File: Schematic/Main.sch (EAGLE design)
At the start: 48 parts, among them IC1 PIC18F4550_40, IC2 7805, IC4 AD7734, IC5 AD780, K1 SRD-24VDC-SL-C, K2 SRD-24VDC-SL-C, Q1 20MHz, Q2 6.144MHz, T1 2N2222, U1 LM317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

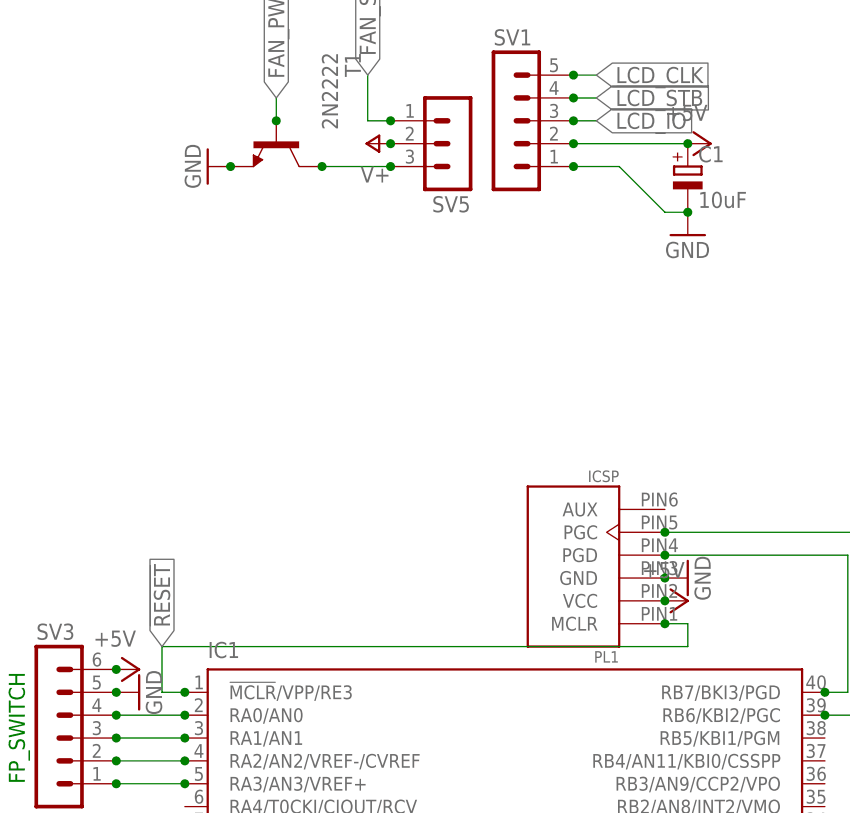
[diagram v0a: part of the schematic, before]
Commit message: Made some changes to capacitor values and such.g
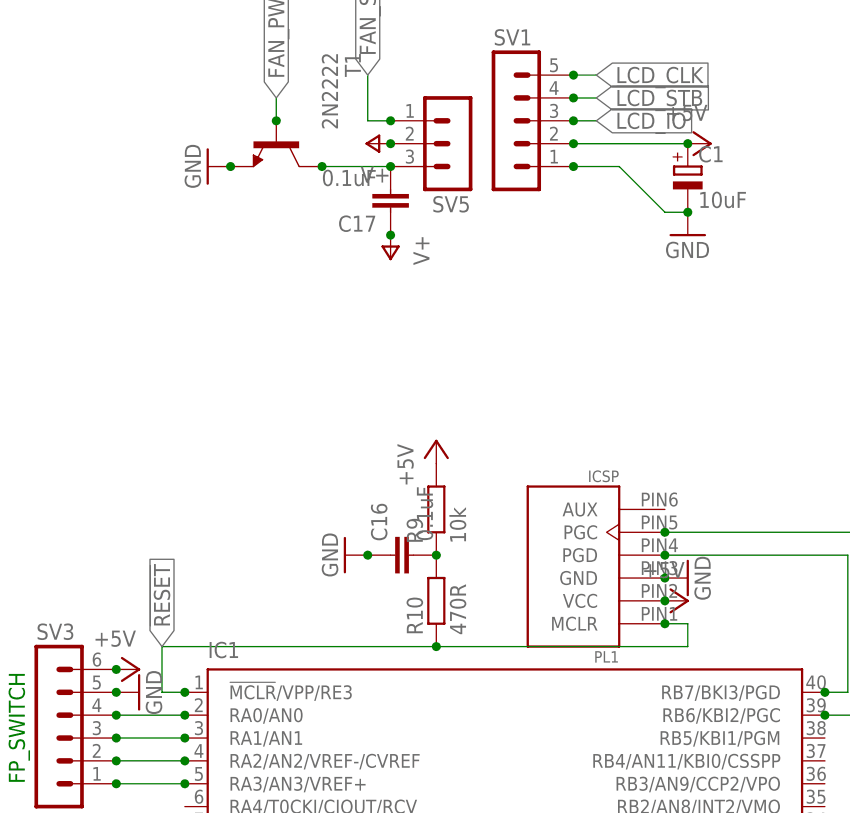
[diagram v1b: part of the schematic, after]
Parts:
- added C16, C17: 0.1uF, rcl:C-EU025-030X050
- added R10: 470R, rcl:R-EU_0204/7
- added R9: 10k, rcl:R-EU_0204/7
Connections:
- new net N$2: C16.2, R10.2, R9.1
- net !RESET!: now also R10.1
- net +5V: now also R9.2
- net GND: now also C16.1
- net N$27: now also C17.2
- net V+: now also C17.1
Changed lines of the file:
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@@
 <part name="AGND7" library="supply1" deviceset="AGND" device=""/>
 <part name="P+18" library="supply1" deviceset="+5V" device=""/>
+<part name="R9" library="rcl" deviceset="R-EU_" device="0204/7" value="10k"/>
+<part name="P+19" library="supply1" deviceset="+5V" device=""/>
+<part name="C17" library="rcl" deviceset="C-EU" device="025-030X050" value="0.1uF"/>
+<part name="P+20" library="supply1" deviceset="V+" device=""/>
+<part name="R10" library="rcl" deviceset="R-EU_" device="0204/7" value="470R"/>
+<part name="C16" library="rcl" deviceset="C-EU" device="025-030X050" value="0.1uF"/>
+<part name="GND23" library="supply1" deviceset="GND" device=""/>
 </parts>
 <sheets>
@@
 <instance part="AGND7" gate="VR1" x="-121.92" y="-43.18"/>
 <instance part="P+18" gate="1" x="-124.46" y="-33.02" rot="R90"/>
+<instance part="R9" gate="G$1" x="-7.62" y="45.72" rot="R90"/>
+<instance part="P+19" gate="1" x="-7.62" y="53.34"/>
+<instance part="C17" gate="G$1" x="-12.7" y="78.74" rot="R180"/>
+<instance part="P+20" gate="1" x="-12.7" y="73.66" rot="R180"/>
+<instance part="R10" gate="G$1" x="-7.62" y="35.56" rot="R90"/>
+<instance part="C16" gate="G$1" x="-12.7" y="40.64" rot="R90"/>
+<instance part="GND23" gate="1" x="-17.78" y="40.64" rot="R270"/>
 </instances>
 <busses>
@@
 <pinref part="P+18" gate="1" pin="+5V"/>
 </segment>
+<segment>
+<pinref part="R9" gate="G$1" pin="2"/>
+<pinref part="P+19" gate="1" pin="+5V"/>
+</segment>
 </net>
 <net name="LCD_IO" class="0">
@@
 <junction x="-175.26" y="-38.1"/>
 </segment>
+<segment>
+<pinref part="C16" gate="G$1" pin="1"/>
+<pinref part="GND23" gate="1" pin="GND"/>
+<junction x="-15.24" y="40.64"/>
+</segment>
 </net>
 <net name="N$1" class="0">
@@
 <pinref part="P+14" gate="1" pin="V+"/>
 <junction x="-12.7" y="86.36"/>
+</segment>
+<segment>
+<pinref part="C17" gate="G$1" pin="1"/>
+<pinref part="P+20" gate="1" pin="V+"/>
+<junction x="-12.7" y="76.2"/>
 </segment>
 </net>
@@
 <junction x="-12.7" y="83.82"/>
 <junction x="-20.32" y="83.82"/>
+<pinref part="C17" gate="G$1" pin="2"/>
 </segment>
 </net>
@@
 <wire x1="-35.56" y1="25.4" x2="-38.1" y2="25.4" width="0.1524" layer="91"/>
 <wire x1="-38.1" y1="25.4" x2="-38.1" y2="30.48" width="0.1524" layer="91"/>
-<wire x1="-38.1" y1="30.48" x2="20.32" y2="30.48" width="0.1524" layer="91"/>
+<wire x1="-38.1" y1="30.48" x2="-7.62" y2="30.48" width="0.1524" layer="91"/>
+<wire x1="-7.62" y1="30.48" x2="20.32" y2="30.48" width="0.1524" layer="91"/>
 <wire x1="20.32" y1="30.48" x2="20.32" y2="33.02" width="0.1524" layer="91"/>
 <pinref part="PL1" gate="G$1" pin="MCLR"/>
@@
 <junction x="-35.56" y="25.4"/>
 <label x="-38.1" y="30.48" size="1.778" layer="95" rot="R90" xref="yes"/>
+<pinref part="R10" gate="G$1" pin="1"/>
+<junction x="-7.62" y="30.48"/>
 </segment>
 </net>
@@
 </segment>
 </net>
+<net name="N$2" class="0">
+<segment>
+<pinref part="R9" gate="G$1" pin="1"/>
+<pinref part="R10" gate="G$1" pin="2"/>
+<pinref part="C16" gate="G$1" pin="2"/>
+<junction x="-7.62" y="40.64"/>
+<pinref part="C16" gate="G$1" pin="2"/>
+</segment>
+</net>

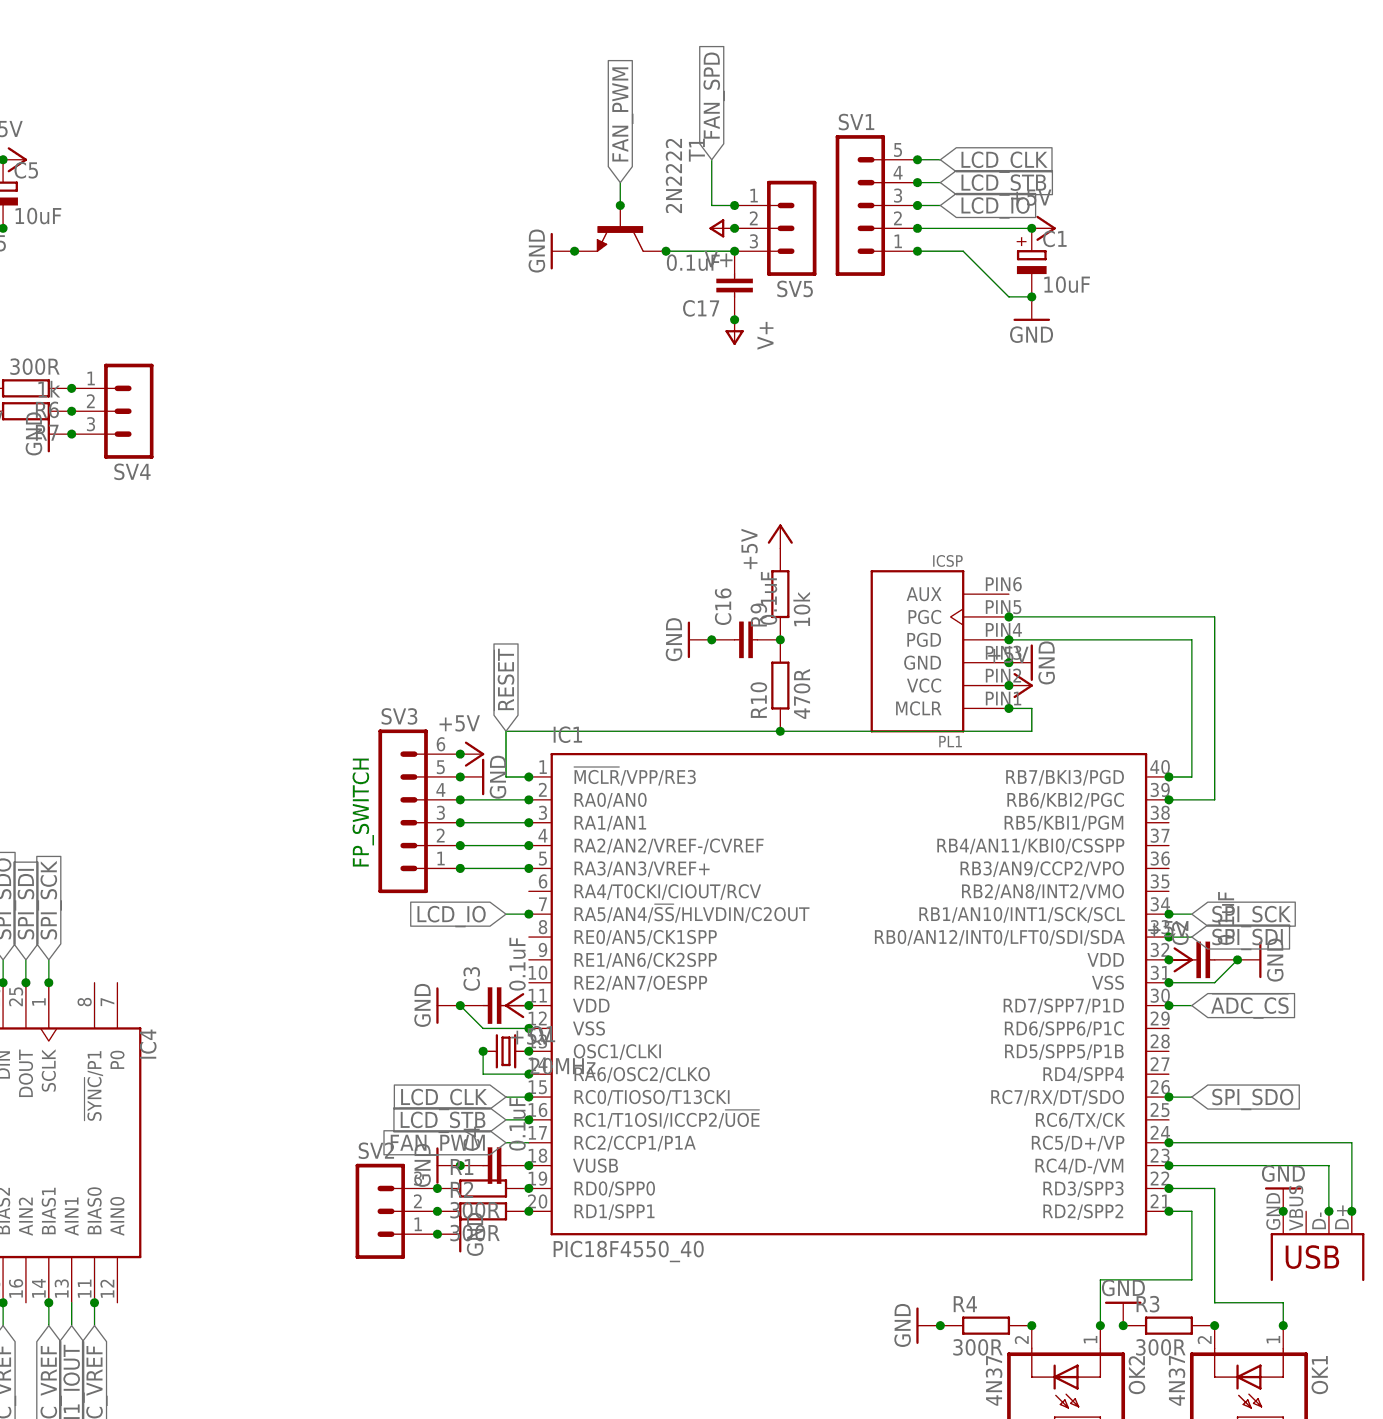
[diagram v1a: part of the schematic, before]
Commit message: Added fan speed pins and temperature socket.
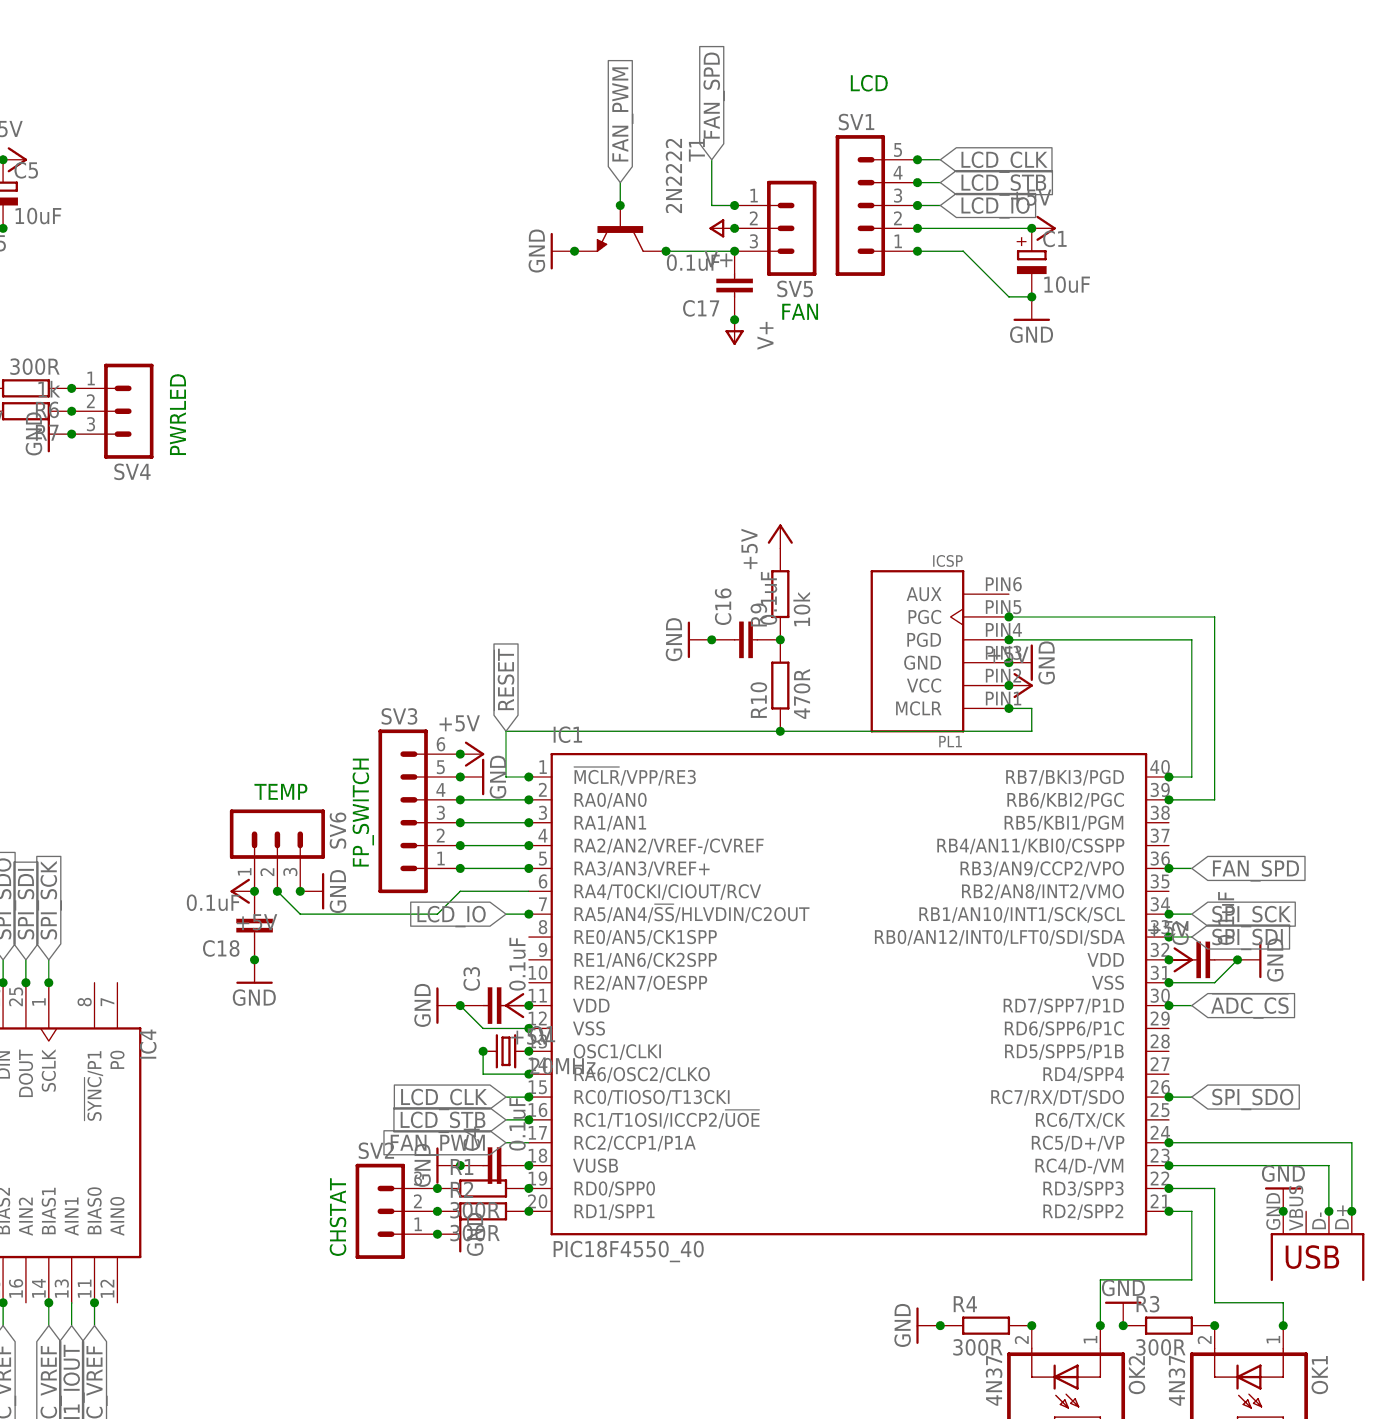
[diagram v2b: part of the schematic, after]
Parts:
- added C18: 0.1uF, rcl:C-EU025-030X050
- added SV6: (no value), con-lstb:MA03-1
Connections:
- new net N$30: IC1.RA4/T0CKI/CIOUT/RCV, SV6.2
- net +5V: now also C18.2, SV6.1
- net FAN_SPD: now also IC1.RB3/AN9/CCP2/VPO
- net GND: now also C18.1, SV6.3
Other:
- note added: "CHSTAT"
- note added: "FAN"
- note added: "LCD"
- note added: "PWRLED"
- note added: "TEMP"
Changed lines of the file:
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@@
 <part name="C16" library="rcl" deviceset="C-EU" device="025-030X050" value="0.1uF"/>
 <part name="GND23" library="supply1" deviceset="GND" device=""/>
+<part name="SV6" library="con-lstb" deviceset="MA03-1" device=""/>
+<part name="P+21" library="supply1" deviceset="+5V" device=""/>
+<part name="GND24" library="supply1" deviceset="GND" device=""/>
+<part name="C18" library="rcl" deviceset="C-EU" device="025-030X050" value="0.1uF"/>
+<part name="GND27" library="supply1" deviceset="GND" device=""/>
 </parts>
 <sheets>
@@
 <plain>
 <text x="-53.34" y="15.24" size="1.778" layer="91" rot="R90">FP_SWITCH</text>
+<text x="-66.04" y="22.86" size="1.778" layer="91">TEMP</text>
+<text x="-55.88" y="-27.94" size="1.778" layer="91" rot="R90">CHSTAT</text>
+<text x="-7.62" y="76.2" size="1.778" layer="91">FAN</text>
+<text x="0" y="101.6" size="1.778" layer="91">LCD</text>
+<text x="-73.66" y="60.96" size="1.778" layer="91" rot="R90">PWRLED</text>
 </plain>
 <instances>
@@
 <instance part="C16" gate="G$1" x="-12.7" y="40.64" rot="R90"/>
 <instance part="GND23" gate="1" x="-17.78" y="40.64" rot="R270"/>
+<instance part="SV6" gate="G$1" x="-63.5" y="20.32" rot="R270"/>
+<instance part="P+21" gate="1" x="-68.58" y="12.7" rot="R90"/>
+<instance part="GND24" gate="1" x="-58.42" y="12.7" rot="R90"/>
+<instance part="C18" gate="G$1" x="-66.04" y="7.62" rot="R180"/>
+<instance part="GND27" gate="1" x="-66.04" y="2.54"/>
 </instances>
 <busses>
@@
 <pinref part="P+19" gate="1" pin="+5V"/>
 </segment>
+<segment>
+<pinref part="SV6" gate="G$1" pin="1"/>
+<pinref part="P+21" gate="1" pin="+5V"/>
+<junction x="-66.04" y="12.7"/>
+<pinref part="C18" gate="G$1" pin="2"/>
+</segment>
 </net>
 <net name="LCD_IO" class="0">
@@
 <pinref part="GND23" gate="1" pin="GND"/>
 <junction x="-15.24" y="40.64"/>
+</segment>
+<segment>
+<pinref part="SV6" gate="G$1" pin="3"/>
+<pinref part="GND24" gate="1" pin="GND"/>
+<junction x="-60.96" y="12.7"/>
+</segment>
+<segment>
+<pinref part="C18" gate="G$1" pin="1"/>
+<pinref part="GND27" gate="1" pin="GND"/>
+<junction x="-66.04" y="5.08"/>
 </segment>
 </net>
@@
 <junction x="-12.7" y="88.9"/>
 </segment>
+<segment>
+<pinref part="IC1" gate="G$1" pin="RB3/AN9/CCP2/VPO"/>
+<wire x1="38.1" y1="15.24" x2="35.56" y2="15.24" width="0.1524" layer="91"/>
+<label x="38.1" y="15.24" size="1.778" layer="95" xref="yes"/>
+<junction x="35.56" y="15.24"/>
+</segment>
 </net>
 <net name="N$27" class="0">
@@
 </segment>
 </net>
+<net name="N$30" class="0">
+<segment>
+<pinref part="IC1" gate="G$1" pin="RA4/T0CKI/CIOUT/RCV"/>
+<wire x1="-35.56" y1="12.7" x2="-43.18" y2="12.7" width="0.1524" layer="91"/>
+<wire x1="-43.18" y1="12.7" x2="-45.72" y2="10.16" width="0.1524" layer="91"/>
+<wire x1="-45.72" y1="10.16" x2="-60.96" y2="10.16" width="0.1524" layer="91"/>
+<pinref part="SV6" gate="G$1" pin="2"/>
+<wire x1="-60.96" y1="10.16" x2="-63.5" y2="12.7" width="0.1524" layer="91"/>
+<junction x="-63.5" y="12.7"/>
+</segment>
+</net>
